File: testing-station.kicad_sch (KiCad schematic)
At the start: 12 parts, among them J1 pyranometer, J2 anemometer, J3 AM2315C, J4 FPC connector, SW1 500SSP1S2M2QEA, U1 TBA_1-0519

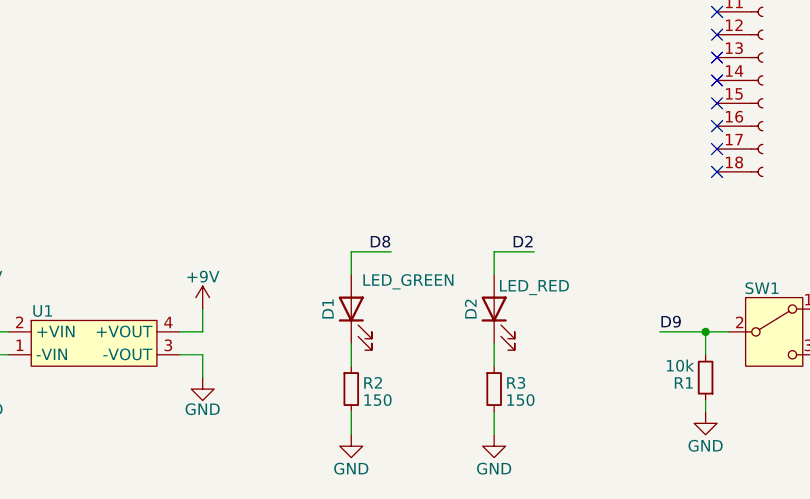
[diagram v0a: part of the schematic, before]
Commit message: MAX31865 routed on PCB
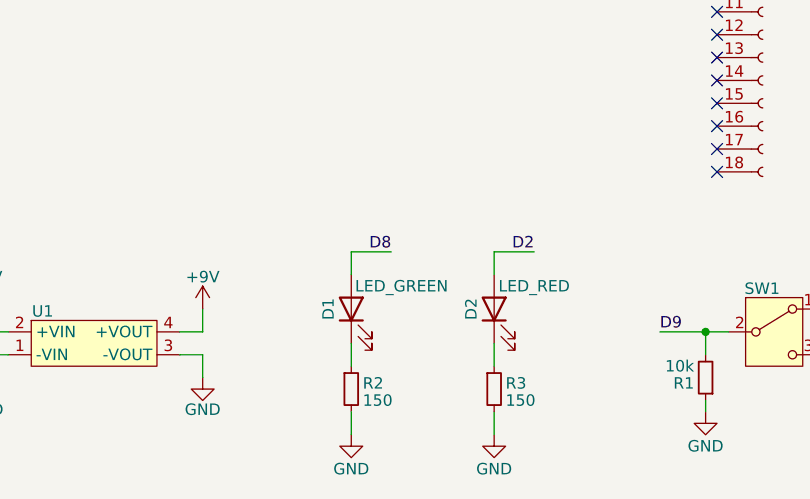
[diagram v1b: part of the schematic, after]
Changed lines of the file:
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@@
 		)
 		(property "Value" "LED_GREEN"
-			(at 82.55 149.225 90)
+			(at 81.788 149.86 90)
 			(effects
 				(font

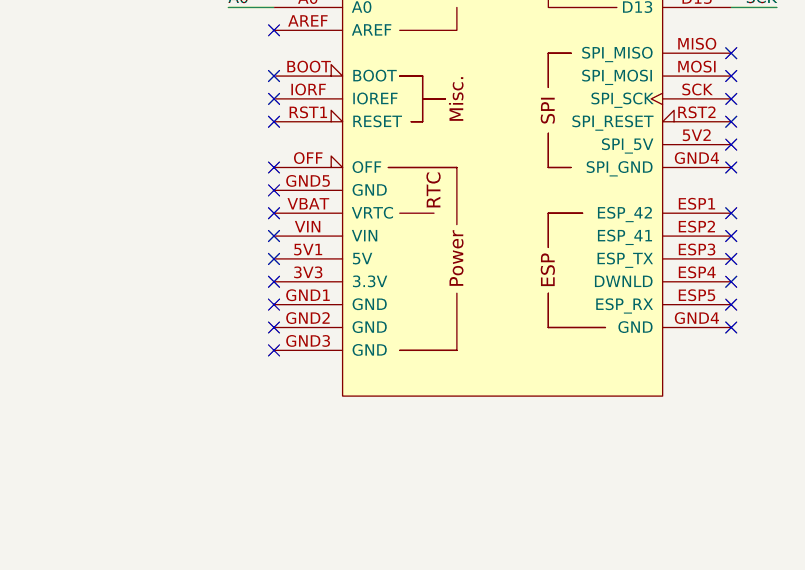
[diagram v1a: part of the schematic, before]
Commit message: DS3231 routed on PCB
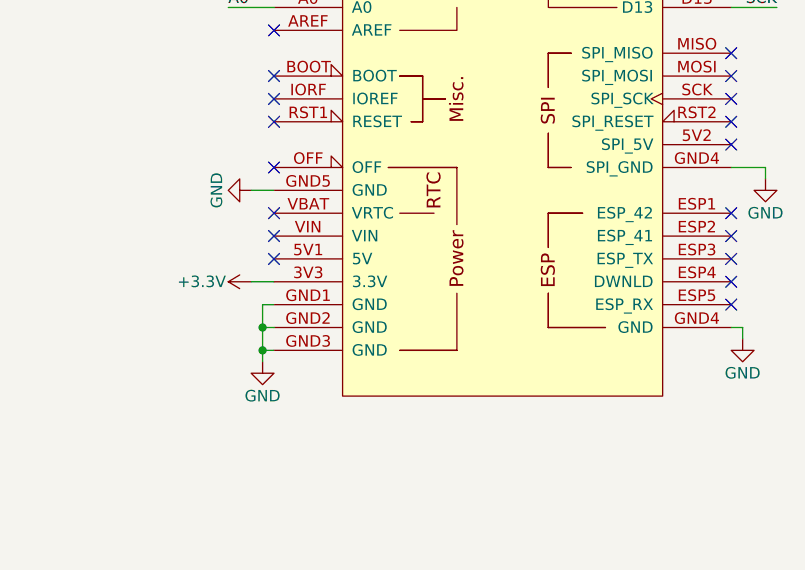
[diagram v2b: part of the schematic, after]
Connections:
- net GND: now also A1.GND1 (GND), A1.GND2 (GND), A1.GND3 (GND), A1.GND4 (SPI_GND), A1.GND5 (GND)
- net +3.3V: now reaches A1.3V3 (3.3V)
- no-connect marks 39 -> 32

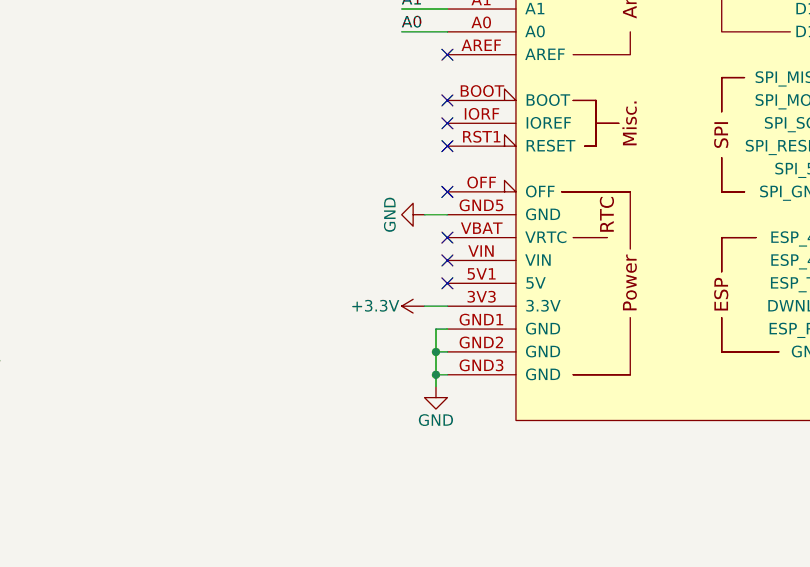
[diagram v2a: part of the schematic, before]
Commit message: BME680 routed on PCB
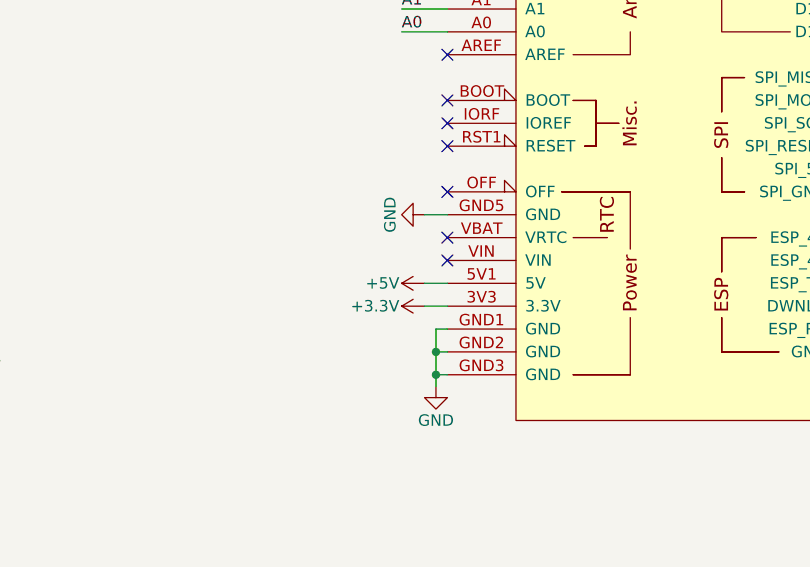
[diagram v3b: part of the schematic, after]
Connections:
- net +5V: now also A1.5V1 (5V)
- no-connect marks 32 -> 31
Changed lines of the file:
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@@
 	)
 	(no_connect
-		(at 185.42 107.95)
-	)
-	(no_connect
 		(at 116.84 137.16)
 	)
@@
 	(wire
 		(pts
+			(xy 182.88 107.95) (xy 185.42 107.95)
+		)
+		(stroke
+			(width 0)
+			(type default)
+		)
+	)
+	(wire
+		(pts
 			(xy 116.84 104.14) (xy 110.49 104.14)
 		)
@@
 					(unit 1)
 				)
+			)
+		)
+	)
+	(symbol
+		(lib_id "power:+5V")
+		(at 182.88 107.95 90)
+		(unit 1)
+		(exclude_from_sim no)
+		(in_bom yes)
+		(on_board yes)
+		(dnp no)
+		(property "Reference" "#PWR051"
+			(at 186.69 107.95 0)
+			(effects
+				(font
+					(size 1.27 1.27)
+				)
+				(hide yes)
+			)
+		)
+		(property "Value" "+5V"
+			(at 180.086 107.95 90)
+			(effects
+				(font
+					(size 1.27 1.27)
+				)
+				(justify left)
+			)
+		)
+		(property "Footprint" ""
+			(at 182.88 107.95 0)
+			(effects
+				(font
+					(size 1.27 1.27)
+				)
+				(hide yes)
+			)
+		)
+		(property "Datasheet" ""
+			(at 182.88 107.95 0)
+			(effects
+				(font
+					(size 1.27 1.27)
+				)
+				(hide yes)
+			)
+		)
+		(property "Description" "Power symbol creates a global label with name \"+5V\""
+			(at 182.88 107.95 0)
+			(effects
+				(font
+					(size 1.27 1.27)
+				)
+				(hide yes)
+			)
+		)
+		(pin "1"
+		)
+		(instances
+			(project "testing-station"
+				(path "/ed3950ec-e24f-4dd6-b9cc-eca012f1333b"
+					(reference "#PWR051")
+					(unit 1)
+				)

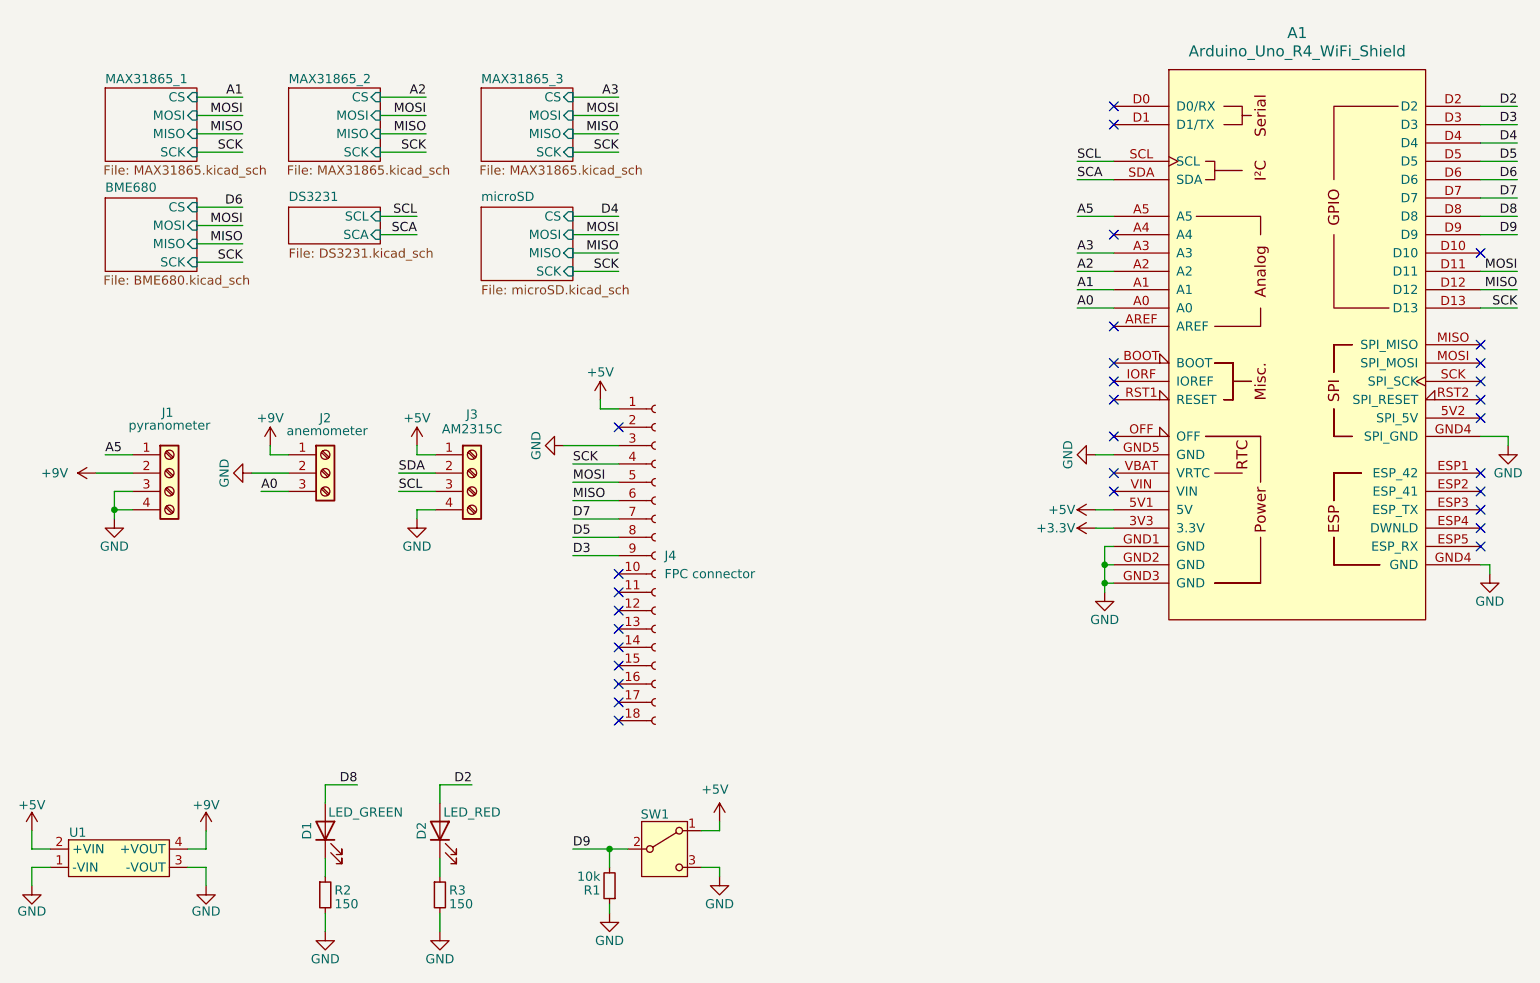
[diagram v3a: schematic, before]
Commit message: changed Arduino symbol to connectors only
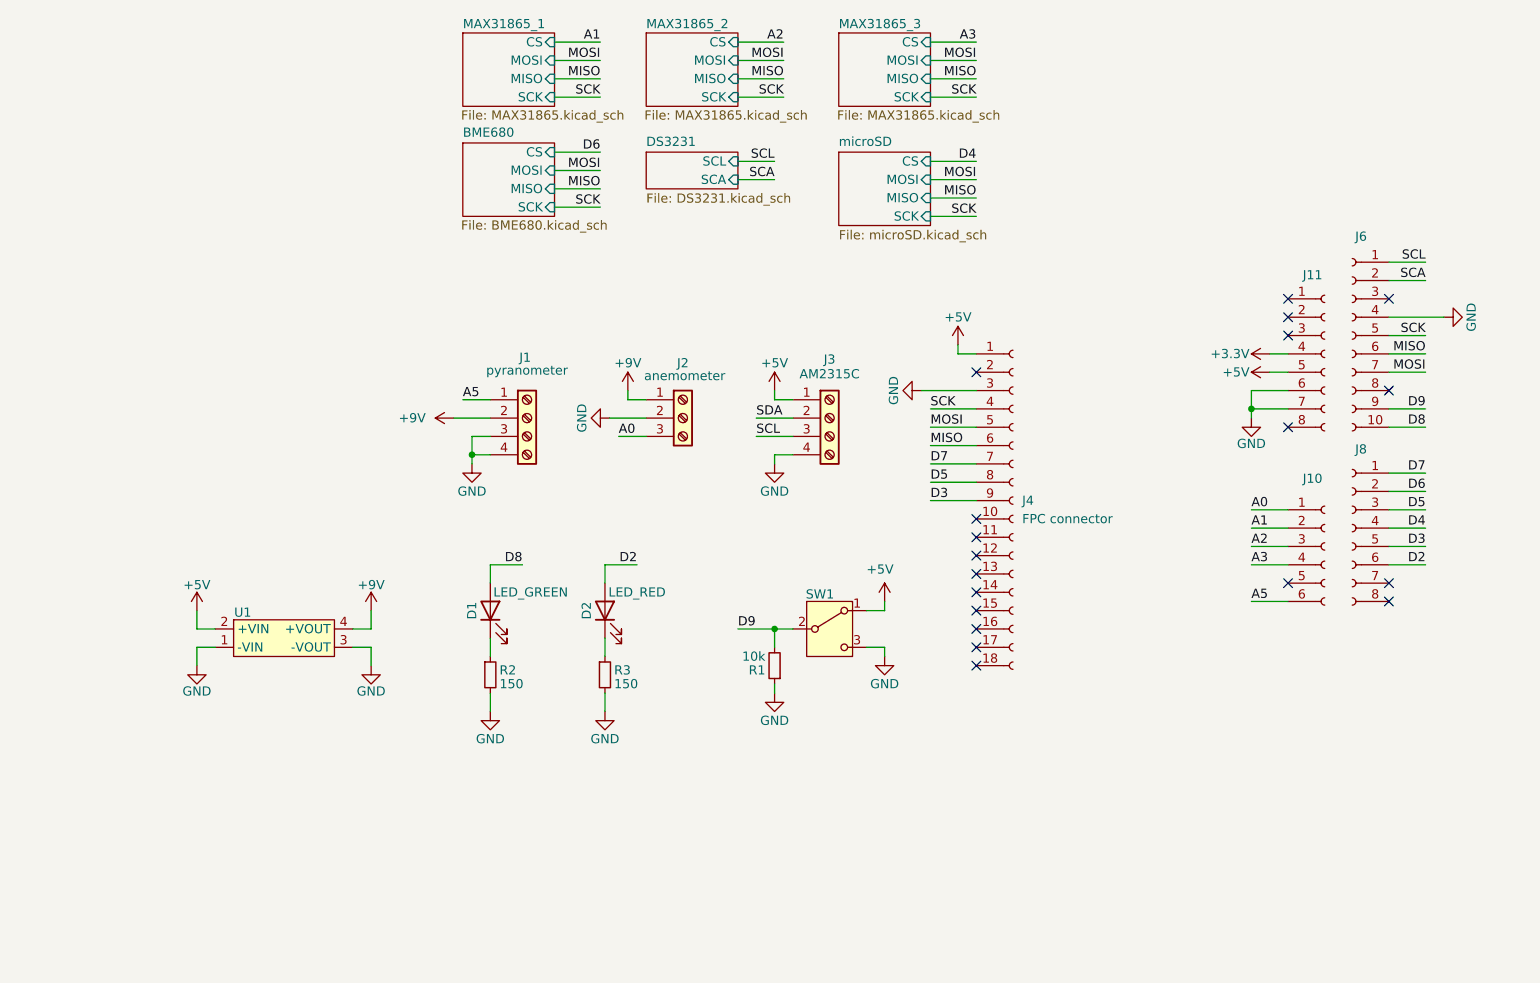
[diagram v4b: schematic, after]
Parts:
- removed A1: Arduino_Uno_R4_WiFi_Shield, PCM_arduino-library:Arduino_Uno_R4_WiFi_Shield, symbol PCM_arduino-library:Arduino_Uno_R4_WiFi_Shield
- added J10: Conn_01x06_Socket, Connector_PinSocket_2.54mm:PinSocket_1x06_P2.54mm_Vertical, symbol Connector:Conn_01x06_Socket
- added J11, J8: Conn_01x08_Socket, Connector_PinSocket_2.54mm:PinSocket_1x08_P2.54mm_Vertical, symbol Connector:Conn_01x08_Socket
- added J6: Conn_01x10_Socket, Connector_PinSocket_2.54mm:PinSocket_1x10_P2.54mm_Vertical, symbol Connector:Conn_01x10_Socket
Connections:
- net +3.3V: now also J11.4 (Pin_4)
- net +5V: now also J11.5 (Pin_5)
- net A0: now also J10.1 (Pin_1)
- net A1: now also J10.2 (Pin_2)
- net A2: now also J10.3 (Pin_3)
- net A3: now also J10.4 (Pin_4)
- net A5: now also J10.6 (Pin_6)
- net D2: now also J8.6 (Pin_6)
- net D3: now also J8.5 (Pin_5)
- net D4: now also J8.4 (Pin_4)
- net D5: now also J8.3 (Pin_3)
- net D6: now also J8.2 (Pin_2)
- net D7: now also J8.1 (Pin_1)
- net D8: now also J6.10 (Pin_10)
- net D9: now also J6.9 (Pin_9)
- net GND: now also J11.6 (Pin_6), J11.7 (Pin_7), J6.4 (Pin_4)
- net MISO: now also J6.6 (Pin_6)
- net MOSI: now also J6.7 (Pin_7)
- net SCA: now also J6.2 (Pin_2)
- net SCK: now also J6.5 (Pin_5)
- net SCL: now also J6.1 (Pin_1)
- no-connect marks 31 -> 19
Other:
- moved on the sheet: D1, D2, J1, J2, J3, J4, R1, R2, R3, SW1, U1

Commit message: finished routing
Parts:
- J1, J3: footprint TerminalBlock:TerminalBlock_bornier-4_P5.08mm -> TerminalBlock_4Ucon:TerminalBlock_4Ucon_1x04_P3.50mm_Horizontal
- J2: footprint TerminalBlock:TerminalBlock_bornier-3_P5.08mm -> TerminalBlock_4Ucon:TerminalBlock_4Ucon_1x03_P3.50mm_Horizontal
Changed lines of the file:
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@@
 			)
 		)
-		(property "Footprint" "TerminalBlock:TerminalBlock_bornier-4_P5.08mm"
+		(property "Footprint" "TerminalBlock_4Ucon:TerminalBlock_4Ucon_1x04_P3.50mm_Horizontal"
 			(at 146.05 95.25 0)
 			(effects
@@
 			)
 		)
-		(property "Footprint" "TerminalBlock:TerminalBlock_bornier-4_P5.08mm"
+		(property "Footprint" "TerminalBlock_4Ucon:TerminalBlock_4Ucon_1x04_P3.50mm_Horizontal"
 			(at 104.14 95.25 0)
 			(effects
@@
 			)
 		)
-		(property "Footprint" "TerminalBlock:TerminalBlock_bornier-3_P5.08mm"
+		(property "Footprint" "TerminalBlock_4Ucon:TerminalBlock_4Ucon_1x03_P3.50mm_Horizontal"
 			(at 125.73 95.25 0)
 			(effects

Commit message: BOM update
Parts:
- D1, D2: Component package type 1206 -> (none)
- J1, J3: MPN 0395430004 -> 0393570004; SPN WM13967-ND -> WM7860-ND
- J10: MPN (none) -> SSQ-106-01-G-S; Manufacturer (none) -> Samtec Inc.; SPN (none) -> SAM1180-06-ND; Supplier (none) -> DigiKey
- J11, J8: MPN (none) -> SSQ-108-01-G-S; Manufacturer (none) -> Samtec Inc.; SPN (none) -> SAM1180-08-ND; Supplier (none) -> DigiKey
- J2: MPN 0395430003 -> 0393570003; SPN WM9752-ND -> WM7878-ND
- J4: Component package type / -> (none)
- J6: MPN (none) -> SSQ-110-01-G-S; Manufacturer (none) -> Samtec Inc.; SPN (none) -> SAM1180-10-ND; Supplier (none) -> DigiKey
- R1, R2, R3: Component package type R_1206 -> (none)
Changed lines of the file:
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@@
 			)
 		)
-		(property "Description" "Generic screw terminal, single row, 01x04, script generated (kicad-library-utils/schlib/autogen/connector/)"
+		(property "Description" "TERM BLK 4POS SIDE ENT 3.5MM PCB"
 			(at 146.05 95.25 0)
 			(effects
@@
 			)
 		)
-		(property "MPN" "0395430004"
+		(property "MPN" "0393570004"
 			(at 146.05 95.25 0)
 			(effects
@@
 			)
 		)
-		(property "SPN" "WM13967-ND"
+		(property "SPN" "WM7860-ND"
 			(at 146.05 95.25 0)
 			(effects
@@
 			)
 		)
-		(property "Description" "Generic screw terminal, single row, 01x04, script generated (kicad-library-utils/schlib/autogen/connector/)"
+		(property "Description" "TERM BLK 4POS SIDE ENT 3.5MM PCB"
 			(at 104.14 95.25 0)
 			(effects
@@
 			)
 		)
-		(property "MPN" "0395430004"
+		(property "MPN" "0393570004"
 			(at 104.14 95.25 0)
 			(effects
@@
 			)
 		)
-		(property "SPN" "WM13967-ND"
+		(property "SPN" "WM7860-ND"
 			(at 104.14 95.25 0)
 			(effects
@@
 			)
 		)
-		(property "Component package type" "R_1206"
-			(at 99.06 130.81 0)
-			(effects
-				(font
-					(size 1.27 1.27)
-				)
-				(hide yes)
-			)
-		)
 		(pin "1"
 		)
@@
 			)
 		)
-		(property "Component package type" "1206"
-			(at 114.935 121.92 0)
-			(effects
-				(font
-					(size 1.27 1.27)
-				)
-				(hide yes)
-			)
-		)
 		(pin "1"
 		)
@@
 			)
 		)
-		(property "Description" "Generic connector, single row, 01x06, script generated"
+		(property "Description" "CONN RCPT 6POS 0.1 GOLD PCB"
+			(at 214.63 113.03 0)
+			(effects
+				(font
+					(size 1.27 1.27)
+				)
+				(hide yes)
+			)
+		)
+		(property "MPN" "SSQ-106-01-G-S"
+			(at 214.63 113.03 0)
+			(effects
+				(font
+					(size 1.27 1.27)
+				)
+				(hide yes)
+			)
+		)
+		(property "Manufacturer" "Samtec Inc."
+			(at 214.63 113.03 0)
+			(effects
+				(font
+					(size 1.27 1.27)
+				)
+				(hide yes)
+			)
+		)
+		(property "SPN" "SAM1180-06-ND"
+			(at 214.63 113.03 0)
+			(effects
+				(font
+					(size 1.27 1.27)
+				)
+				(hide yes)
+			)
+		)
+		(property "Supplier" "DigiKey"
 			(at 214.63 113.03 0)
 			(effects
@@
 			)
 		)
-		(property "Component package type" "R_1206"
-			(at 114.935 130.81 0)
-			(effects
-				(font
-					(size 1.27 1.27)
-				)
-				(hide yes)
-			)
-		)
 		(pin "1"
 		)
@@
 		)
 		(property "SPN" "732-4993-1-ND"
-			(at 99.06 121.92 0)
-			(effects
-				(font
-					(size 1.27 1.27)
-				)
-				(hide yes)
-			)
-		)
-		(property "Component package type" "1206"
 			(at 99.06 121.92 0)
 			(effects
@@
 			)
 		)
-		(property "Description" "Generic connector, single row, 01x10, script generated"
+		(property "Description" "CONN RCPT 10POS 0.1 GOLD PCB"
+			(at 218.44 83.82 0)
+			(effects
+				(font
+					(size 1.27 1.27)
+				)
+				(hide yes)
+			)
+		)
+		(property "MPN" "SSQ-110-01-G-S"
+			(at 218.44 83.82 0)
+			(effects
+				(font
+					(size 1.27 1.27)
+				)
+				(hide yes)
+			)
+		)
+		(property "Manufacturer" "Samtec Inc."
+			(at 218.44 83.82 0)
+			(effects
+				(font
+					(size 1.27 1.27)
+				)
+				(hide yes)
+			)
+		)
+		(property "SPN" "SAM1180-10-ND"
+			(at 218.44 83.82 0)
+			(effects
+				(font
+					(size 1.27 1.27)
+				)
+				(hide yes)
+			)
+		)
+		(property "Supplier" "DigiKey"
 			(at 218.44 83.82 0)
 			(effects
@@
 			)
 		)
-		(property "Description" "Generic screw terminal, single row, 01x03, script generated (kicad-library-utils/schlib/autogen/connector/)"
+		(property "Description" "TERM BLK 3POS SIDE ENT 3.5MM PCB"
 			(at 125.73 95.25 0)
 			(effects
@@
 			)
 		)
-		(property "MPN" "0395430003"
+		(property "MPN" "0393570003"
 			(at 125.73 95.25 0)
 			(effects
@@
 			)
 		)
-		(property "SPN" "WM9752-ND"
+		(property "SPN" "WM7878-ND"
 			(at 125.73 95.25 0)
 			(effects
@@
 			)
 		)
-		(property "Description" "Generic connector, single row, 01x08, script generated"
+		(property "Description" "CONN RCPT 8POS 0.1 GOLD PCB"
+			(at 218.44 110.49 0)
+			(effects
+				(font
+					(size 1.27 1.27)
+				)
+				(hide yes)
+			)
+		)
+		(property "MPN" "SSQ-108-01-G-S"
+			(at 218.44 110.49 0)
+			(effects
+				(font
+					(size 1.27 1.27)
+				)
+				(hide yes)
+			)
+		)
+		(property "Manufacturer" "Samtec Inc."
+			(at 218.44 110.49 0)
+			(effects
+				(font
+					(size 1.27 1.27)
+				)
+				(hide yes)
+			)
+		)
+		(property "SPN" "SAM1180-08-ND"
+			(at 218.44 110.49 0)
+			(effects
+				(font
+					(size 1.27 1.27)
+				)
+				(hide yes)
+			)
+		)
+		(property "Supplier" "DigiKey"
 			(at 218.44 110.49 0)
 			(effects
@@
 			)
 		)
-		(property "Component package type" "/"
-			(at 171.45 106.68 0)
-			(effects
-				(font
-					(size 1.27 1.27)
-				)
-				(hide yes)
-			)
-		)
 		(property "Manufacturer" "Omron Electronics Inc-EMC Div"
 			(at 171.45 106.68 0)
@@
 			)
 		)
-		(property "Component package type" "R_1206"
-			(at 138.43 129.54 0)
-			(effects
-				(font
-					(size 1.27 1.27)
-				)
-				(hide yes)
-			)
-		)
 		(pin "1"
 		)
@@
 			)
 		)
-		(property "Description" "Generic connector, single row, 01x08, script generated"
+		(property "Description" "CONN RCPT 8POS 0.1 GOLD PCB"
 			(at 214.63 86.36 0)
 			(effects
+				(font
+					(size 1.27 1.27)
+				)
+				(hide yes)
+			)
+		)
+		(property "MPN" "SSQ-108-01-G-S"
+			(at 214.63 86.36 0)
+			(effects
+				(font
+					(size 1.27 1.27)
+				)
+				(hide yes)
+			)
+		)
+		(property "Manufacturer" "Samtec Inc."
+			(at 214.63 86.36 0)
+			(effects
+				(font
+					(size 1.27 1.27)
+				)
+				(hide yes)
+			)
+		)
+		(property "SPN" "SAM1180-08-ND"
+			(at 214.63 86.36 0)
+			(effects
+				(font
+					(size 1.27 1.27)
+				)
+				(hide yes)
+			)
+		)
+		(property "Supplier" "DigiKey"
+			(at 214.63 86.36 0)
+			(effects

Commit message: update README.md
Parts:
- J1, J3: MPN 0393570004 -> 039357-0004
- J2: MPN 0393570003 -> 039357-0003
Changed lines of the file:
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@@
 			)
 		)
-		(property "MPN" "0393570004"
+		(property "MPN" "039357-0004"
 			(at 146.05 95.25 0)
 			(effects
@@
 			)
 		)
-		(property "MPN" "0393570004"
+		(property "MPN" "039357-0004"
 			(at 104.14 95.25 0)
 			(effects
@@
 			)
 		)
-		(property "MPN" "0393570003"
+		(property "MPN" "039357-0003"
 			(at 125.73 95.25 0)
 			(effects
